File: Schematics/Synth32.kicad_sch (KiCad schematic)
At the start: 1 part

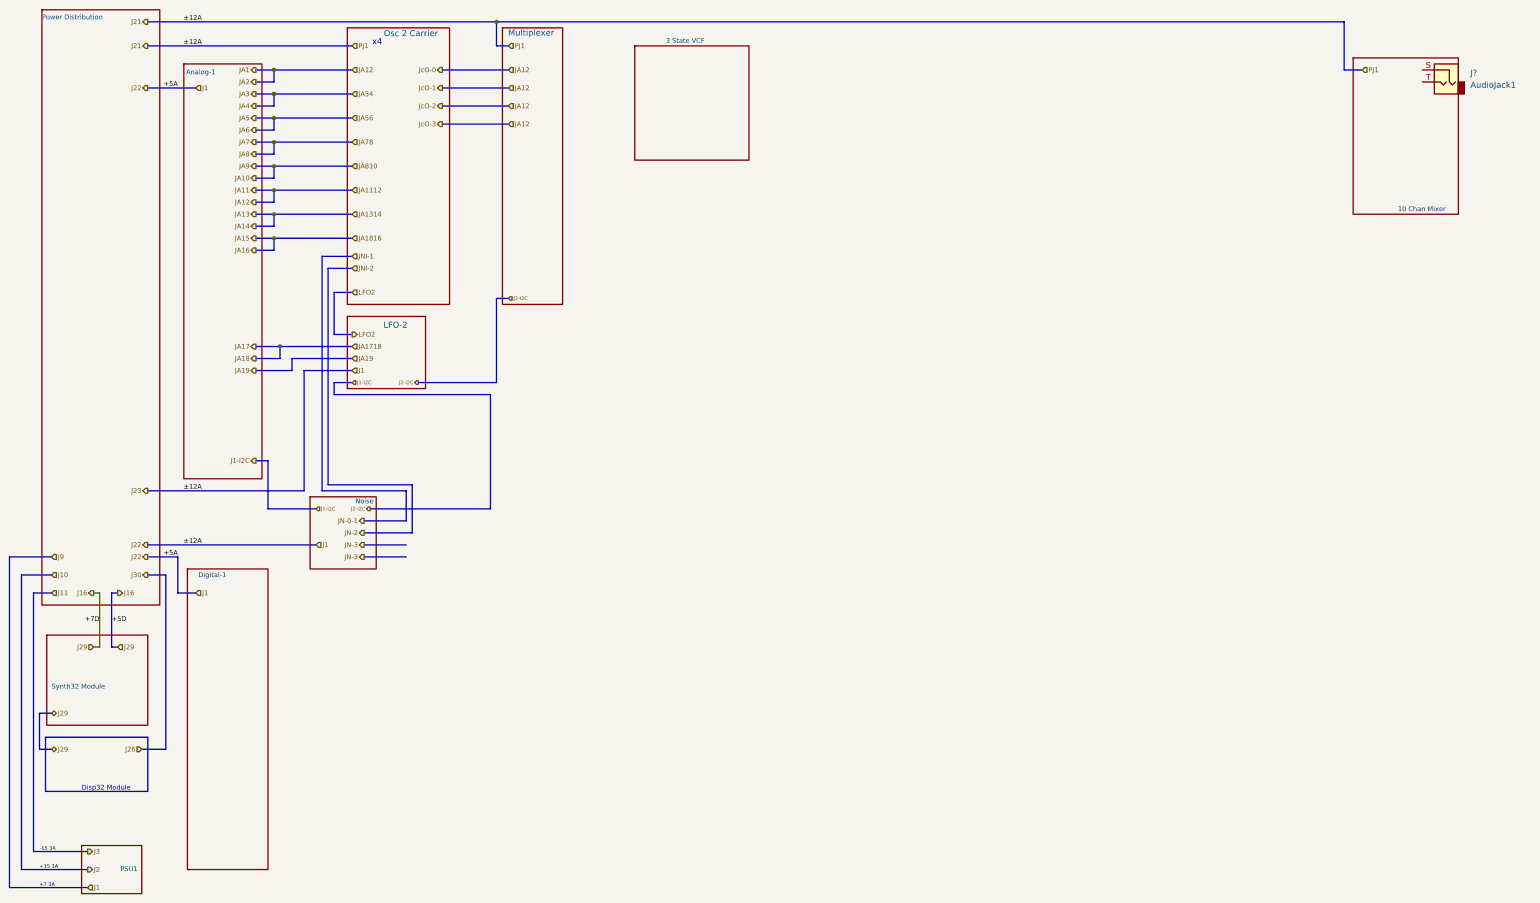
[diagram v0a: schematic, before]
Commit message: Updated schematics including VCO and VCF daughter boards
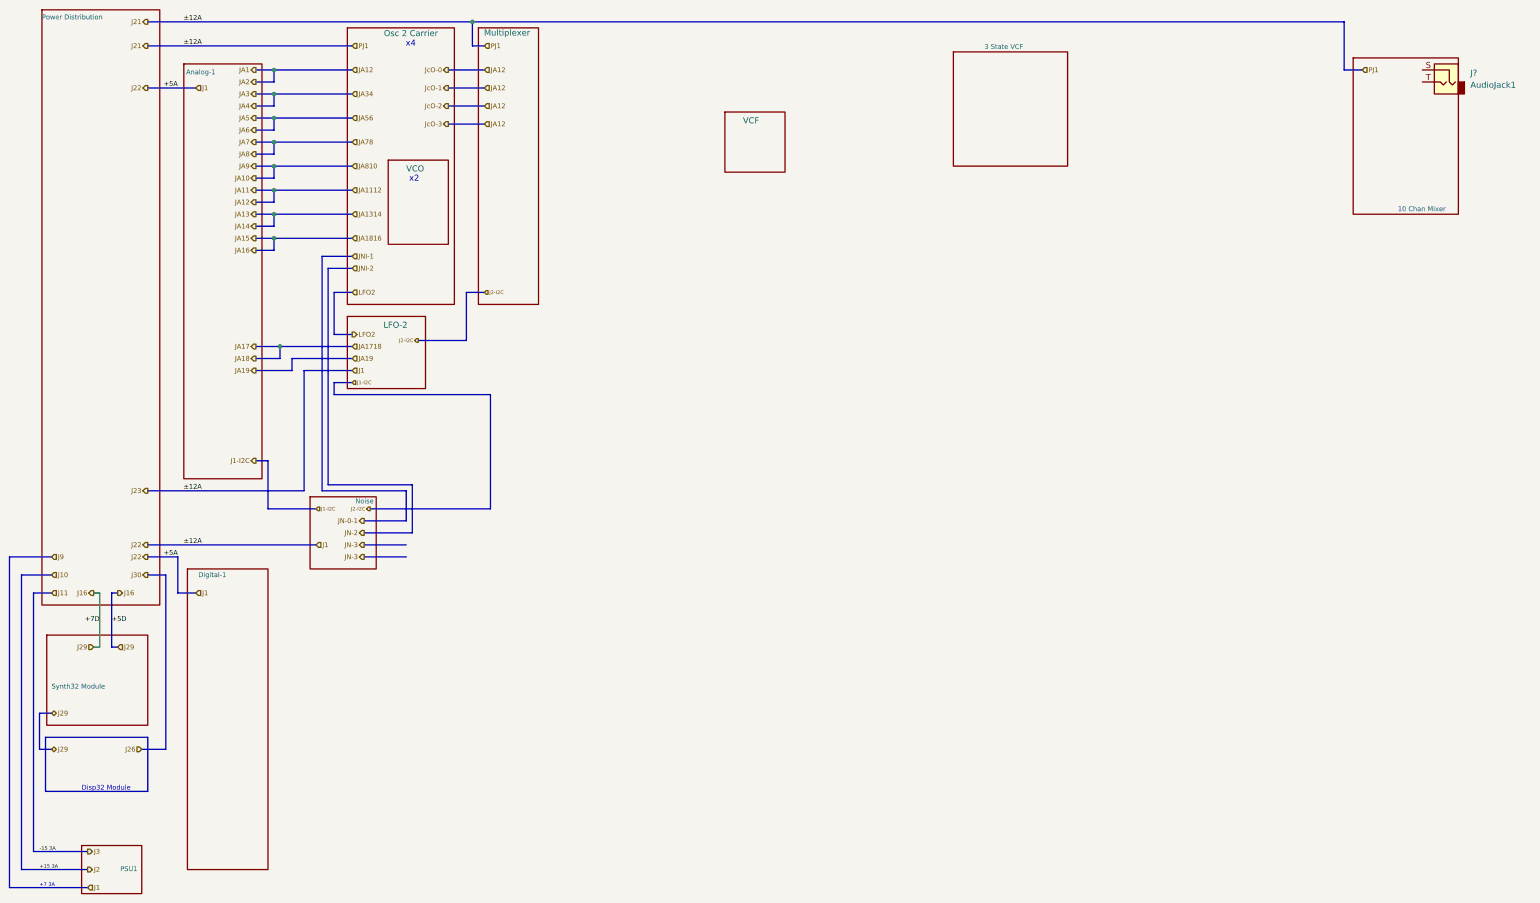
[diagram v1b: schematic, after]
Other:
- added sheet VCF (VCF.kicad_sch)
- added sheet VCO (VCO.kicad_sch)
- note added: "x2"
- company:       MLE Tech                  Cedar Park, TX -> (none)
- title: Synth #2 -> Top Interconnect
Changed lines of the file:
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@@
 	(paper "USLegal")
 	(title_block
-		(title "Synth #2")
-		(date "2023-07-27")
-		(rev "0.1")
-		(company "      MLE Tech                  Cedar Park, TX")
-		(comment 2 "In Development")
-	)
-	(junction
-		(at 116.84 16.51)
-		(diameter 0)
-		(color 0 0 0 0)
+		(title "Top Interconnect")
+		(date "2025-01-16")
+		(rev "3.2")
+		(comment 1 "In Development ")
 	)
 	(junction
@@
 	)
 	(junction
+		(at 111.76 16.51)
+		(diameter 0)
+		(color 0 0 0 0)
+	)
+	(junction
 		(at 71.12 85.09)
 		(diameter 0)
@@
 	(bus
 		(pts
-			(xy 116.84 16.51) (xy 295.91 16.51)
-		)
-		(stroke
-			(width 0)
-			(type default)
-		)
-	)
-	(bus
-		(pts
-			(xy 116.84 16.51) (xy 116.84 21.59)
+			(xy 111.76 16.51) (xy 111.76 21.59)
+		)
+		(stroke
+			(width 0)
+			(type default)
+		)
+	)
+	(bus
+		(pts
+			(xy 111.76 16.51) (xy 295.91 16.51)
 		)
 		(stroke
@@
 	(bus
 		(pts
-			(xy 105.41 38.1) (xy 119.38 38.1)
+			(xy 106.68 38.1) (xy 114.3 38.1)
 		)
 		(stroke
@@
 	(bus
 		(pts
-			(xy 100.33 92.71) (xy 116.84 92.71)
+			(xy 100.33 83.82) (xy 110.49 83.82)
 		)
 		(stroke
@@
 	(bus
 		(pts
-			(xy 116.84 21.59) (xy 119.38 21.59)
+			(xy 111.76 21.59) (xy 114.3 21.59)
 		)
 		(stroke
@@
 	(bus
 		(pts
-			(xy 43.18 16.51) (xy 116.84 16.51)
-		)
-		(stroke
-			(width 0)
-			(type default)
-		)
-	)
-	(bus
-		(pts
-			(xy 105.41 30.48) (xy 119.38 30.48)
+			(xy 43.18 16.51) (xy 111.76 16.51)
+		)
+		(stroke
+			(width 0)
+			(type default)
+		)
+	)
+	(bus
+		(pts
+			(xy 106.68 30.48) (xy 114.3 30.48)
 		)
 		(stroke
@@
 	(bus
 		(pts
-			(xy 105.41 34.29) (xy 119.38 34.29)
+			(xy 106.68 34.29) (xy 114.3 34.29)
 		)
 		(stroke
@@
 	(bus
 		(pts
-			(xy 116.84 74.93) (xy 119.38 74.93)
+			(xy 110.49 73.66) (xy 114.3 73.66)
 		)
 		(stroke
@@
 	(bus
 		(pts
-			(xy 116.84 92.71) (xy 116.84 74.93)
+			(xy 110.49 83.82) (xy 110.49 73.66)
 		)
 		(stroke
@@
 	(bus
 		(pts
-			(xy 105.41 26.67) (xy 119.38 26.67)
+			(xy 106.68 26.67) (xy 114.3 26.67)
 		)
 		(stroke
@@
 		)
 	)
+	(text "x2"
+		(exclude_from_sim no)
+		(at 99.468 49.724 0)
+		(effects
+			(font
+				(size 1.27 1.27)
+			)
+		)
+	)
 	(text "x4"
 		(exclude_from_sim no)
-		(at 91.6383 20.8709 0)
+		(at 98.7267 21.1927 0)
 		(effects
 			(font
@@
 	(hierarchical_label "J2-I2C"
 		(shape input)
-		(at 119.38 74.93 0)
+		(at 114.3 73.66 0)
 		(fields_autoplaced yes)
 		(effects
@@
 	(hierarchical_label "JcO-2"
 		(shape output)
-		(at 105.41 34.29 180)
+		(at 106.68 34.29 180)
 		(fields_autoplaced yes)
 		(effects
@@
 	(hierarchical_label "JA12"
 		(shape input)
-		(at 119.38 38.1 0)
+		(at 114.3 38.1 0)
 		(fields_autoplaced yes)
 		(effects
@@
 	(hierarchical_label "JcO-3"
 		(shape output)
-		(at 105.41 38.1 180)
+		(at 106.68 38.1 180)
 		(fields_autoplaced yes)
 		(effects
@@
 	(hierarchical_label "J2-I2C"
 		(shape output)
-		(at 100.33 92.71 180)
+		(at 100.33 83.82 180)
 		(fields_autoplaced yes)
 		(effects
@@
 	(hierarchical_label "JA12"
 		(shape input)
-		(at 119.38 26.67 0)
+		(at 114.3 26.67 0)
 		(fields_autoplaced yes)
 		(effects
@@
 	(hierarchical_label "JcO-0"
 		(shape output)
-		(at 105.41 26.67 180)
+		(at 106.68 26.67 180)
 		(fields_autoplaced yes)
 		(effects
@@
 	(hierarchical_label "JA12"
 		(shape input)
-		(at 119.38 30.48 0)
+		(at 114.3 30.48 0)
 		(fields_autoplaced yes)
 		(effects
@@
 	(hierarchical_label "JA12"
 		(shape input)
-		(at 119.38 34.29 0)
+		(at 114.3 34.29 0)
 		(fields_autoplaced yes)
 		(effects
@@
 	(hierarchical_label "JcO-1"
 		(shape output)
-		(at 105.41 30.48 180)
+		(at 106.68 30.48 180)
 		(fields_autoplaced yes)
 		(effects
@@
 	(hierarchical_label "PJ1"
 		(shape input)
-		(at 119.38 21.59 0)
+		(at 114.3 21.59 0)
 		(fields_autoplaced yes)
 		(effects
@@
 		)
 		(instances
-			(project "Schematics-Midi32"
+			(project "Synth32"
 				(path "/718f017d-28fe-4e29-b548-40db8e21cec7"
 					(page "2")
@@
 		)
 		(instances
-			(project "Schematics-Midi32"
+			(project "Synth32"
 				(path "/718f017d-28fe-4e29-b548-40db8e21cec7"
-					(page "9")
+					(page "11")
 				)
 			)
@@
 	)
 	(sheet
-		(at 118.11 17.78)
+		(at 113.03 17.78)
 		(size 12.7 58.42)
 		(stroke
@@
 		)
 		(property "Sheetname" "Multiplexer"
-			(at 119.2881 19.5544 0)
+			(at 114.2081 19.5544 0)
 			(effects
 				(font
@@
 		)
 		(property "Sheetfile" "Multiplexer.kicad_sch"
-			(at 118.11 71.7046 0)
+			(at 113.03 71.7046 0)
 			(effects
 				(font
@@
 		)
 		(instances
-			(project "Schematics-Midi32"
+			(project "Synth32"
 				(path "/718f017d-28fe-4e29-b548-40db8e21cec7"
 					(page "10")
@@
 		)
 		(instances
-			(project "Schematics-Midi32"
+			(project "Synth32"
 				(path "/718f017d-28fe-4e29-b548-40db8e21cec7"
 					(page "6")
@@
 		)
 		(instances
-			(project "Schematics-Midi32"
+			(project "Synth32"
 				(path "/718f017d-28fe-4e29-b548-40db8e21cec7"
 					(page "5")
@@
 		)
 		(instances
-			(project "Schematics-Midi32"
+			(project "Synth32"
 				(path "/718f017d-28fe-4e29-b548-40db8e21cec7"
 					(page "4")
@@
 	)
 	(sheet
-		(at 146.05 21.59)
+		(at 213.36 22.86)
 		(size 24.13 24.13)
 		(stroke
@@
 		)
 		(property "Sheetname" "3 State VCF"
-			(at 156.718 21.082 0)
+			(at 224.028 22.352 0)
 			(effects
 				(font
@@
 		)
 		(property "Sheetfile" "3PoleStateVarVCF.kicad_sch"
-			(at 146.05 46.3046 0)
+			(at 213.36 47.5746 0)
 			(effects
 				(font
@@
 		)
 		(instances
-			(project "Schematics-Midi32"
+			(project "Synth32"
 				(path "/718f017d-28fe-4e29-b548-40db8e21cec7"
 					(page "12")
@@
 		)
 		(instances
-			(project "Schematics-Midi32"
+			(project "Synth32"
 				(path "/718f017d-28fe-4e29-b548-40db8e21cec7"
 					(page "3")
@@
 		)
 		(instances
-			(project "Schematics-Midi32"
+			(project "Synth32"
+				(path "/718f017d-28fe-4e29-b548-40db8e21cec7"
+					(page "14")
+				)
+			)
+		)
+	)
+	(sheet
+		(at 93.98 45.72)
+		(size 12.7 17.78)
+		(stroke
+			(width 0.1524)
+			(type solid)
+		)
+		(fill
+			(color 0 0 0 0.0000)
+		)
+		(property "Sheetname" "VCO"
+			(at 97.79 48.26 0)
+			(effects
+				(font
+					(size 1.27 1.27)
+				)
+				(justify left bottom)
+			)
+		)
+		(property "Sheetfile" "VCO.kicad_sch"
+			(at 93.98 64.0846 0)
+			(effects
+				(font
+					(size 1.27 1.27)
+				)
+				(justify left top)
+				(hide yes)
+			)
+		)
+		(instances
+			(project "Synth32"
 				(path "/718f017d-28fe-4e29-b548-40db8e21cec7"
 					(page "8")
@@
 		)
 		(instances
-			(project "Schematics-Midi32"
+			(project "Synth32"
 				(path "/718f017d-28fe-4e29-b548-40db8e21cec7"
-					(page "11")
+					(page "9")
+				)
+			)
+		)
+	)
+	(sheet
+		(at 165.1 35.56)
+		(size 12.7 12.7)
+		(stroke
+			(width 0.1524)
+			(type solid)
+		)
+		(fill
+			(color 0 0 0 0.0000)
+		)
+		(property "Sheetname" "VCF"
+			(at 168.91 38.1 0)
+			(effects
+				(font
+					(size 1.27 1.27)
+				)
+				(justify left bottom)
+			)
+		)
+		(property "Sheetfile" "VCF.kicad_sch"
+			(at 165.1 48.8446 0)
+			(effects
+				(font
+					(size 1.27 1.27)
+				)
+				(justify left top)
+				(hide yes)
+			)
+		)
+		(instances
+			(project "Synth32"
+				(path "/718f017d-28fe-4e29-b548-40db8e21cec7"
+					(page "13")
 				)
 			)
@@
 	(sheet
 		(at 85.344 17.78)
-		(size 21.59 58.42)
+		(size 22.606 58.42)
 		(stroke
 			(width 0.1524)
@@
 		)
 		(instances
-			(project "Schematics-Midi32"
+			(project "Synth32"
 				(path "/718f017d-28fe-4e29-b548-40db8e21cec7"
 					(page "7")

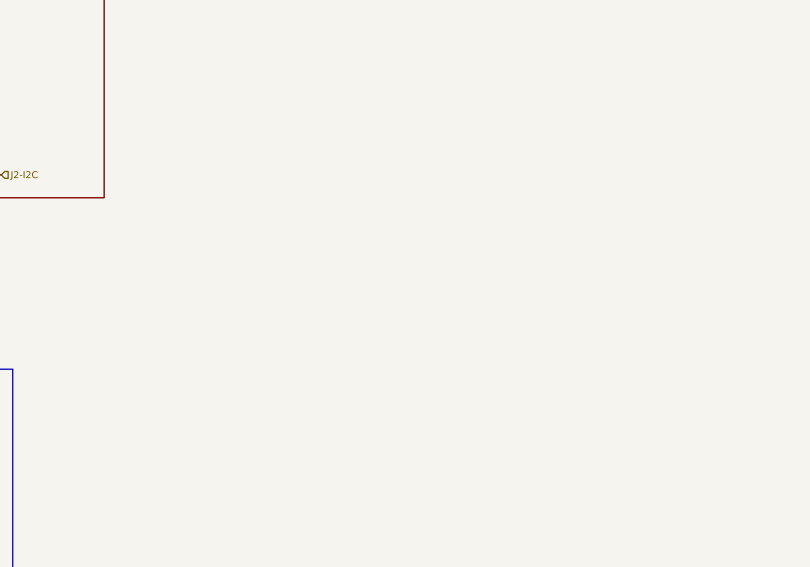
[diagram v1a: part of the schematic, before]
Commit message: Cleaned up page advance on display controls.
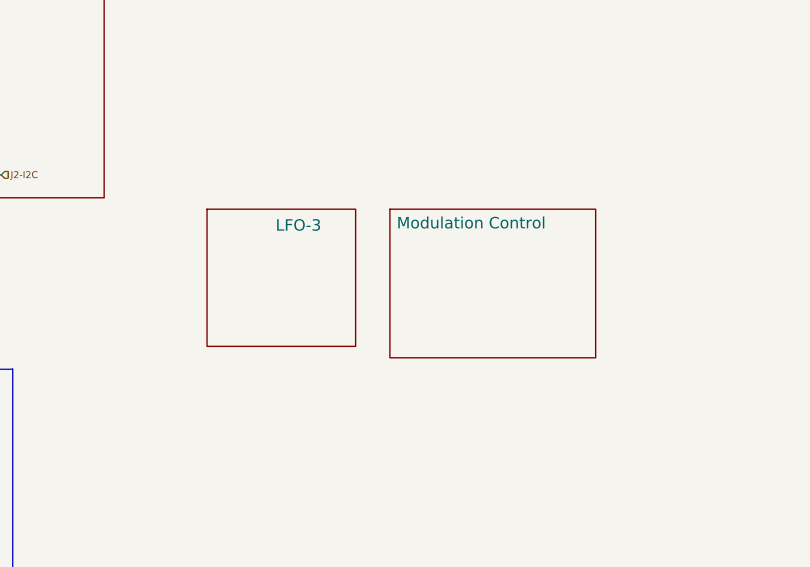
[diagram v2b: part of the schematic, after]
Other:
- added sheet LFO-3 (LFO-2.kicad_sch)
- added sheet Modulation Control (ModControl.kicad_sch)

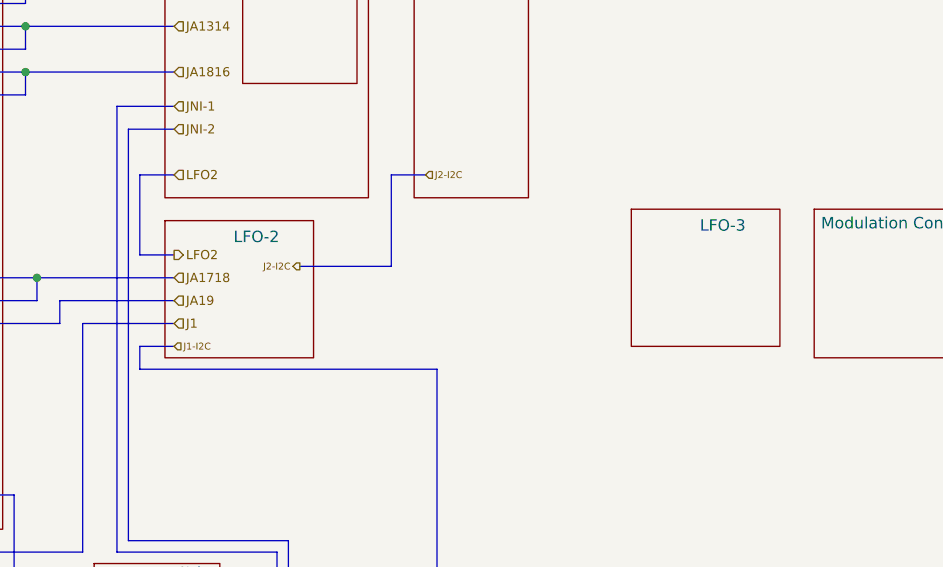
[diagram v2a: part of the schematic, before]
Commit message: minor adjustments for modulation control interface.
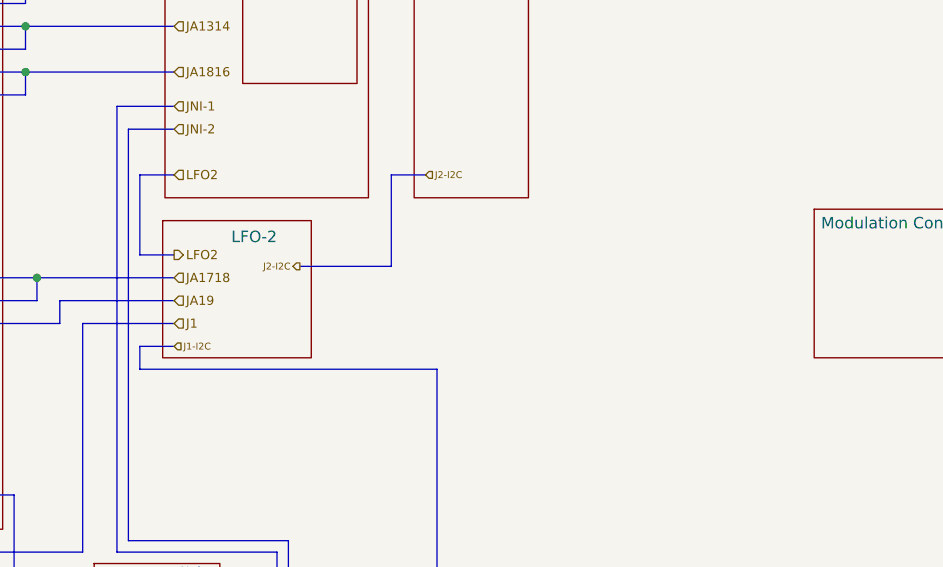
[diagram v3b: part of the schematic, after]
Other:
- removed sheet LFO-3
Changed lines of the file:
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@@
 			(project "Synth32"
 				(path "/718f017d-28fe-4e29-b548-40db8e21cec7"
-					(page "11")
-				)
-			)
-		)
-	)
-	(sheet
-		(at 137.16 77.47)
+					(page "15")
+				)
+			)
+		)
+	)
+	(sheet
+		(at 85.09 78.74)
 		(size 16.51 15.24)
 		(exclude_from_sim no)
@@
 			(color 0 0 0 0.0000)
 		)
-		(property "Sheetname" "LFO-3"
-			(at 144.78 80.01 0)
+		(property "Sheetname" "LFO-2"
+			(at 92.71 81.28 0)
 			(effects
 				(font
@@
 		)
 		(property "Sheetfile" "LFO-2.kicad_sch"
-			(at 137.16 96.5966 0)
-			(effects
-				(font
-					(size 1.27 1.27)
-				)
-				(justify left top)
-				(hide yes)
-			)
-		)
-		(instances
-			(project "Synth32"
-				(path "/718f017d-28fe-4e29-b548-40db8e21cec7"
-					(page "15")
+			(at 85.09 97.8666 0)
+			(effects
+				(font
+					(size 1.27 1.27)
+				)
+				(justify left top)
+				(hide yes)
+			)
+		)
+		(instances
+			(project "Synth32"
+				(path "/718f017d-28fe-4e29-b548-40db8e21cec7"
+					(page "10")
 				)
 			)
@@
 			(project "Synth32"
 				(path "/718f017d-28fe-4e29-b548-40db8e21cec7"
-					(page "10")
+					(page "14")
 				)
 			)
@@
 			(project "Synth32"
 				(path "/718f017d-28fe-4e29-b548-40db8e21cec7"
-					(page "16")
+					(page "11")
 				)
 			)
@@
 				)
 			)
-		)
-	)
-	(sheet
-		(at 85.344 78.74)
-		(size 16.51 15.24)
-		(exclude_from_sim no)
-		(in_bom yes)
-		(on_board yes)
-		(dnp no)
-		(stroke
-			(width 0.1524)
-			(type solid)
-		)
-		(fill
-			(color 0 0 0 0.0000)
-		)
-		(property "Sheetname" "LFO-2"
-			(at 92.964 81.28 0)
-			(effects
-				(font
-					(size 1.27 1.27)
-				)
-				(justify left bottom)
-			)
-		)
-		(property "Sheetfile" "LFO-2.kicad_sch"
-			(at 85.344 97.8666 0)
-			(effects
-				(font
-					(size 1.27 1.27)
-				)
-				(justify left top)
-				(hide yes)
-			)
-		)
-		(instances
-			(project "Synth32"
-				(path "/718f017d-28fe-4e29-b548-40db8e21cec7"
-					(page "14")
-				)
-			)
